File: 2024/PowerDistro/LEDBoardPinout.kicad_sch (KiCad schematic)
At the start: 34 parts, among them U1 PCA9685

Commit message: saved i guess idk
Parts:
- C1: footprint (none) -> Capacitor_SMD:C_0603_1608Metric
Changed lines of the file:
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@@
 			)
 		)
-		(property "Footprint" ""
+		(property "Footprint" "Capacitor_SMD:C_0603_1608Metric"
 			(at 152.0952 85.09 0)
 			(effects

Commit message: Added EASYBldc Outlines
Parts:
- JP4: footprint SM06B-GHS-TB_LF__SN_:JST_SM06B-GHS-TB_LF__SN_ -> PowerDistroFootprints:JST_SM06B-GHS-TB_LF__SN_
- U1: footprint PCA9685:TSSOP28 -> PowerDistroFootprints:TSSOP28
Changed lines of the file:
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@@
 			)
 		)
-		(property "Footprint" "PCA9685:TSSOP28"
+		(property "Footprint" "PowerDistroFootprints:TSSOP28"
 			(at 191.77 90.17 0)
 			(effects
@@
 			)
 		)
-		(property "Footprint" "SM06B-GHS-TB_LF__SN_:JST_SM06B-GHS-TB_LF__SN_"
+		(property "Footprint" "PowerDistroFootprints:JST_SM06B-GHS-TB_LF__SN_"
 			(at 133.35 161.29 0)
 			(effects

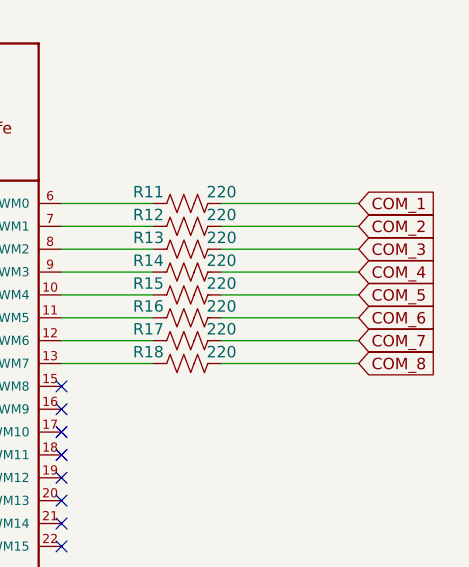
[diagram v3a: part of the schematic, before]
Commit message: Added connectors and esc footprints
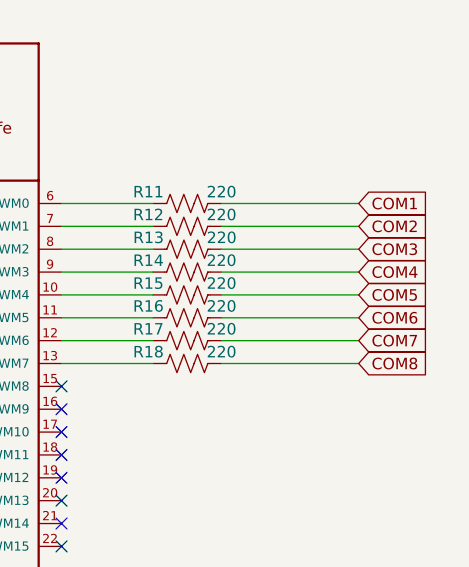
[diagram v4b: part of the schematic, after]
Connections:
- net COM_1 renamed COM1
- net COM_2 renamed COM2
- net COM_3 renamed COM3
- net COM_4 renamed COM4
- net COM_5 renamed COM5
- net COM_6 renamed COM6
- net COM_7 renamed COM7
- net COM_8 renamed COM8
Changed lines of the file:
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@@
 		)
 	)
-	(global_label "COM_6"
+	(global_label "COM6"
 		(shape input)
 		(at 245.11 87.63 0)
@@
 		)
 		(property "Intersheetrefs" "${INTERSHEET_REFS}"
-			(at 254.3242 87.63 0)
+			(at 253.3566 87.63 0)
 			(effects
 				(font
@@
 		)
 	)
-	(global_label "COM_8"
+	(global_label "COM8"
 		(shape input)
 		(at 245.11 92.71 0)
@@
 		)
 		(property "Intersheetrefs" "${INTERSHEET_REFS}"
-			(at 254.3242 92.71 0)
+			(at 253.3566 92.71 0)
 			(effects
 				(font
@@
 		)
 	)
-	(global_label "COM_2"
+	(global_label "COM2"
 		(shape input)
 		(at 245.11 77.47 0)
@@
 		)
 		(property "Intersheetrefs" "${INTERSHEET_REFS}"
-			(at 254.3242 77.47 0)
+			(at 253.3566 77.47 0)
 			(effects
 				(font
@@
 		)
 	)
-	(global_label "COM_1"
+	(global_label "COM1"
 		(shape input)
 		(at 245.11 74.93 0)
@@
 		)
 		(property "Intersheetrefs" "${INTERSHEET_REFS}"
-			(at 254.3242 74.93 0)
-			(effects
-				(font
-					(size 1.27 1.27)
-				)
-				(justify left)
-				(hide yes)
-			)
-		)
-	)
-	(global_label "COM_7"
+			(at 253.3566 74.93 0)
+			(effects
+				(font
+					(size 1.27 1.27)
+				)
+				(justify left)
+				(hide yes)
+			)
+		)
+	)
+	(global_label "COM7"
 		(shape input)
 		(at 245.11 90.17 0)
@@
 		)
 		(property "Intersheetrefs" "${INTERSHEET_REFS}"
-			(at 254.3242 90.17 0)
+			(at 253.3566 90.17 0)
 			(effects
 				(font
@@
 		)
 	)
-	(global_label "COM_5"
+	(global_label "COM5"
 		(shape input)
 		(at 245.11 85.09 0)
@@
 		)
 		(property "Intersheetrefs" "${INTERSHEET_REFS}"
-			(at 254.3242 85.09 0)
+			(at 253.3566 85.09 0)
 			(effects
 				(font
@@
 		)
 	)
-	(global_label "COM_3"
+	(global_label "COM3"
 		(shape input)
 		(at 245.11 80.01 0)
@@
 		)
 		(property "Intersheetrefs" "${INTERSHEET_REFS}"
-			(at 254.3242 80.01 0)
-			(effects
-				(font
-					(size 1.27 1.27)
-				)
-				(justify left)
-				(hide yes)
-			)
-		)
-	)
-	(global_label "COM_4"
+			(at 253.3566 80.01 0)
+			(effects
+				(font
+					(size 1.27 1.27)
+				)
+				(justify left)
+				(hide yes)
+			)
+		)
+	)
+	(global_label "COM4"
 		(shape input)
 		(at 245.11 82.55 0)
@@
 		)
 		(property "Intersheetrefs" "${INTERSHEET_REFS}"
-			(at 254.3242 82.55 0)
-			(effects
-				(font
+			(at 253.3566 82.55 0)
+			(effects
+				(font

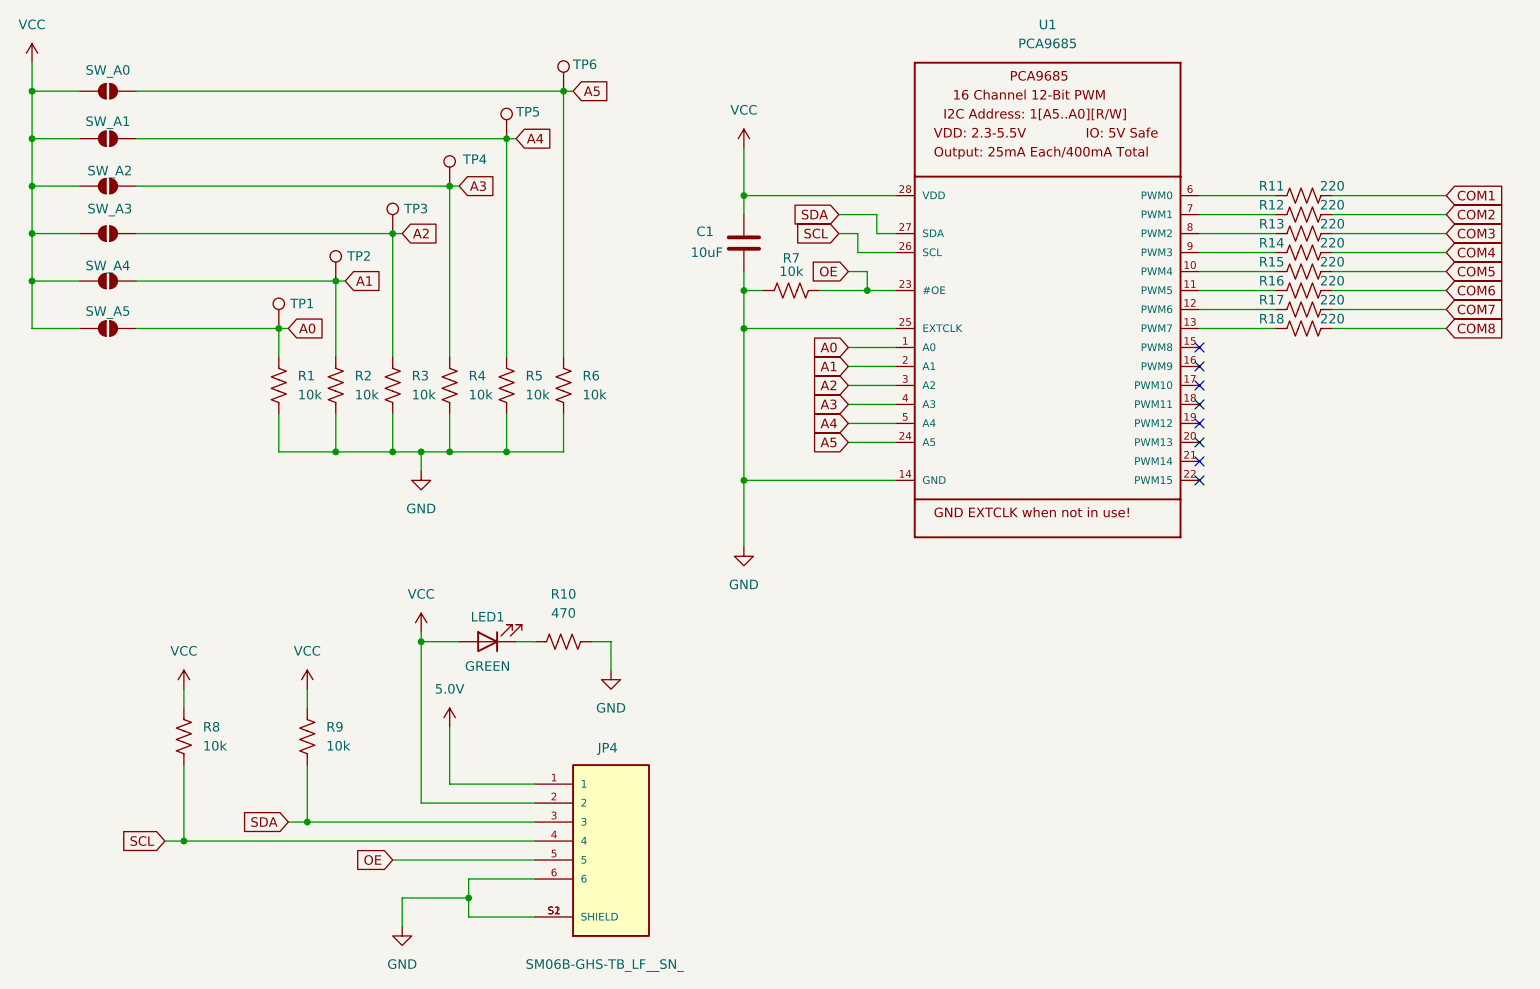
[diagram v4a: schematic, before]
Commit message: Added power layer to power distro motors
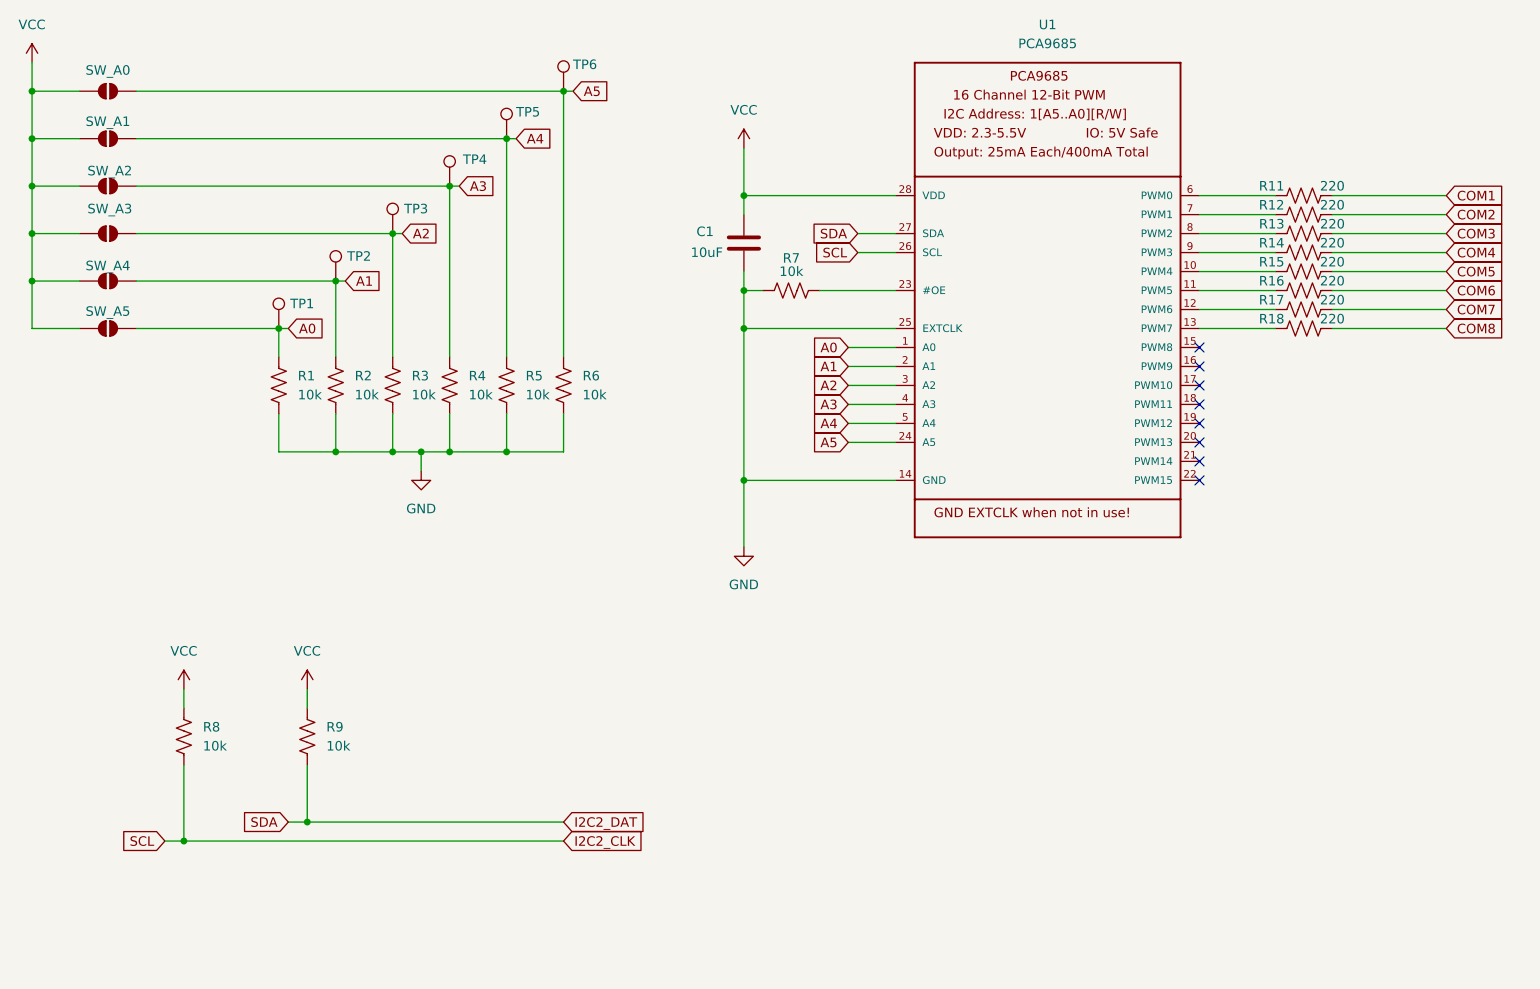
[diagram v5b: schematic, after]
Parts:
- removed JP4: SM06B-GHS-TB_LF__SN_, PowerDistroFootprints:JST_SM06B-GHS-TB_LF__SN_, symbol PowerDistro:SM06B-GHS-TB_LF__SN_
- removed LED1: GREEN, LED_SMD:LED_0603_1608Metric, symbol Device:LED
- removed R10: 470, Resistor_SMD:R_0603_1608Metric, symbol Device:R_US
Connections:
- net OE: no longer names the net of R7.1, U1.23 (#OE)
- net SCL renamed I2C2_CLK
- net SDA renamed I2C2_DAT

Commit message: wired the PCA and Orin connecter together and added motor controller comms
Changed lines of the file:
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@@
+	)
+	(junction
+		(at 151.13 73.66)
+		(diameter 0)
+		(color 0 0 0 0)
 	)
 	(junction
@@
 	(wire
 		(pts
-			(xy 151.13 68.58) (xy 151.13 74.93)
+			(xy 151.13 68.58) (xy 151.13 73.66)
 		)
 		(stroke
@@
 	(wire
 		(pts
+			(xy 147.32 73.66) (xy 151.13 73.66)
+		)
+		(stroke
+			(width 0)
+			(type default)
+		)
+	)
+	(wire
+		(pts
 			(xy 88.9 92.71) (xy 69.85 92.71)
 		)
@@
 		(pts
 			(xy 88.9 92.71) (xy 90.17 92.71)
+		)
+		(stroke
+			(width 0)
+			(type default)
+		)
+	)
+	(wire
+		(pts
+			(xy 151.13 73.66) (xy 151.13 74.93)
 		)
 		(stroke
@@
 				(hide yes)
 			)
+		)
+	)
+	(global_label "3.3_VDC"
+		(shape input)
+		(at 147.32 73.66 180)
+		(fields_autoplaced yes)
+		(effects
+			(font
+				(size 1.27 1.27)
+			)
+			(justify right)
+		)
+		(property "Intersheetrefs" "${INTERSHEET_REFS}"
+			(at 136.7148 73.66 0)
+			(effects
+				(font
+					(size 1.27 1.27)
+				)
+				(justify right)
+				(hide yes)
+			)

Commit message: Changed Everything
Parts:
- removed TP1, TP2, TP3, TP4, TP5, TP6: TestPoint, TestPoint:TestPoint_Pad_D2.5mm, symbol Connector:TestPoint
- added R10, R19, R20, R21, R22, R23, R24, R25: 220, Resistor_SMD:R_0603_1608Metric, symbol Device:R_US
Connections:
- net at U1.15 (PWM8): now also R10.1
- net at U1.16 (PWM9): now also R19.1
- net at U1.17 (PWM10): now also R25.1
- net at U1.18 (PWM11): now also R20.1
- net at U1.19 (PWM12): now also R21.1
- net at U1.20 (PWM13): now also R22.1
- net at U1.21 (PWM14): now also R23.1
- net at U1.22 (PWM15): now also R24.1
- net COM1 renamed PWM1
- net COM2 renamed PWM2
- net COM3 renamed PWM3
- net COM4 renamed PWM4
- net COM5 renamed PWM5
- net COM6 renamed PWM6
- net COM7 renamed PWM7
- net COM8 renamed PWM8
- new net PWM10: R19.2
- new net PWM11: R25.2
- new net PWM12: R20.2
- new net PWM13: R21.2
- new net PWM14: R22.2
- new net PWM15: R23.2
- new net PWM16: R24.2
- new net PWM9: R10.2
- no-connect marks 8 -> 0

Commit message: Release
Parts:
- C1: footprint Capacitor_SMD:C_0603_1608Metric -> Capacitor_SMD:C_1206_3216Metric
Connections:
- net I2C2_CLK renamed I2C_CLK
- net I2C2_DAT renamed I2C_DAT
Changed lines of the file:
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@@
 		)
 	)
-	(global_label "I2C2_CLK"
+	(global_label "I2C_CLK"
 		(shape input)
 		(at 127 161.29 0)
@@
 		)
 		(property "Intersheetrefs" "${INTERSHEET_REFS}"
-			(at 138.8147 161.29 0)
+			(at 137.6052 161.29 0)
 			(effects
 				(font
@@
 		)
 	)
-	(global_label "I2C2_DAT"
+	(global_label "I2C_DAT"
 		(shape input)
 		(at 127 158.75 0)
@@
 		)
 		(property "Intersheetrefs" "${INTERSHEET_REFS}"
-			(at 138.5728 158.75 0)
+			(at 137.3633 158.75 0)
 			(effects
 				(font
@@
 			)
 		)
-		(property "Footprint" "Capacitor_SMD:C_0603_1608Metric"
+		(property "Footprint" "Capacitor_SMD:C_1206_3216Metric"
 			(at 152.0952 85.09 0)
 			(effects
